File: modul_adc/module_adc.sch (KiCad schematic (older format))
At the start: 26 parts

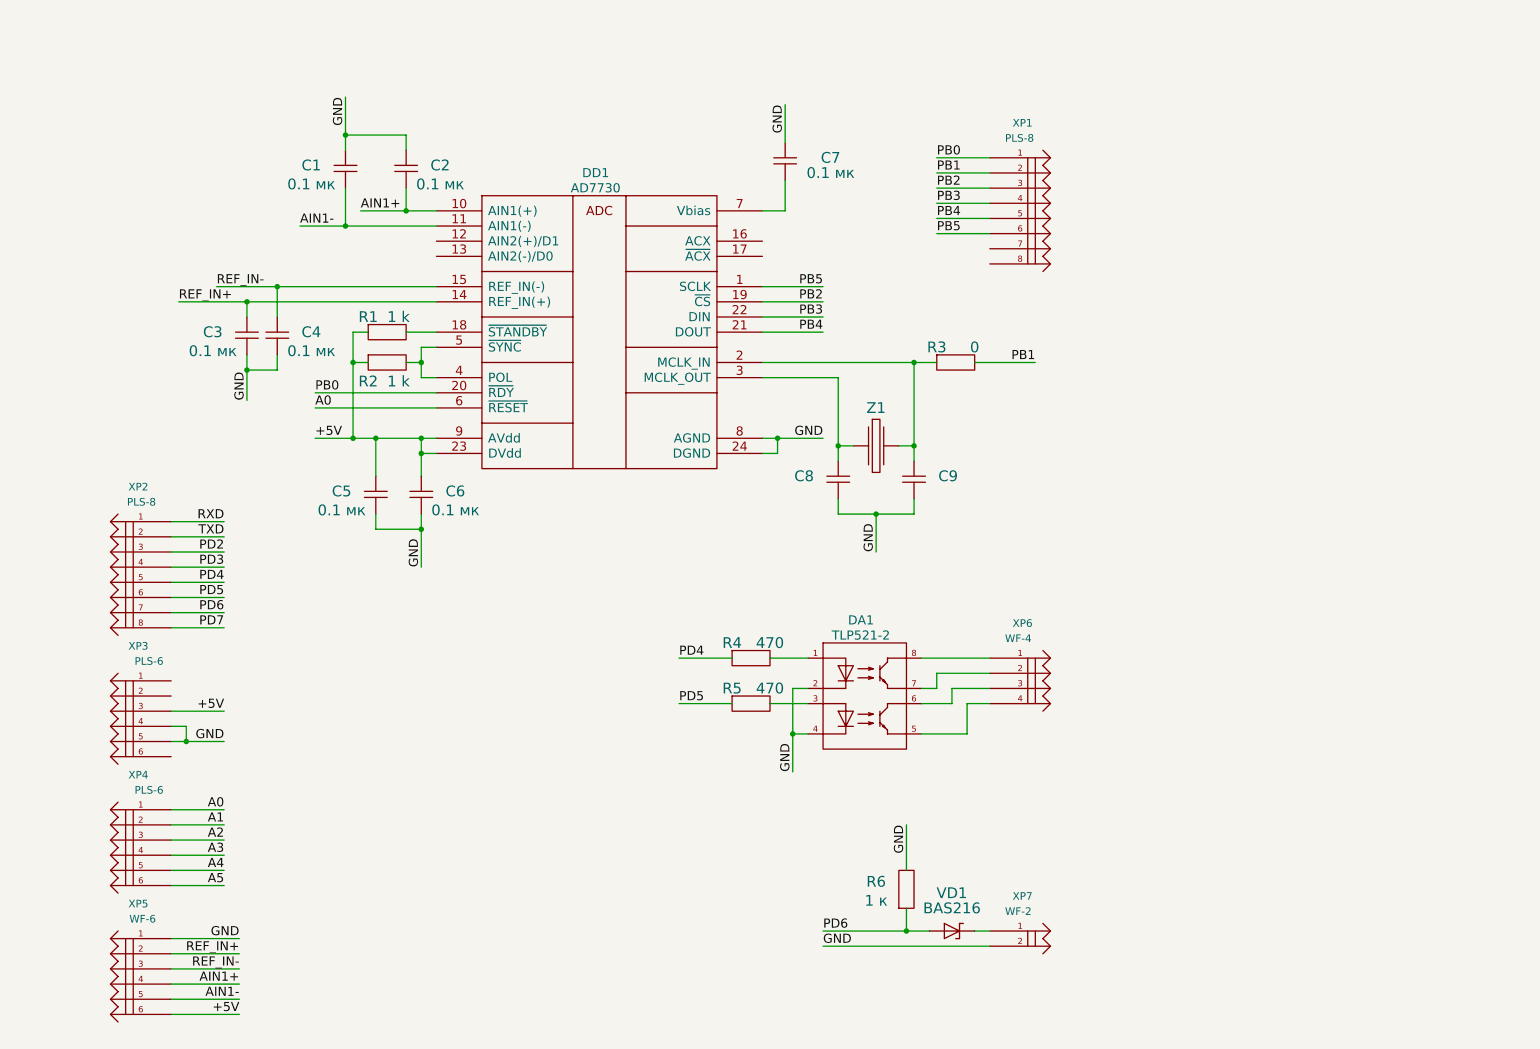
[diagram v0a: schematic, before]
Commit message: Поправил шелкографию и добавил номиналы у элементов для adc_module.
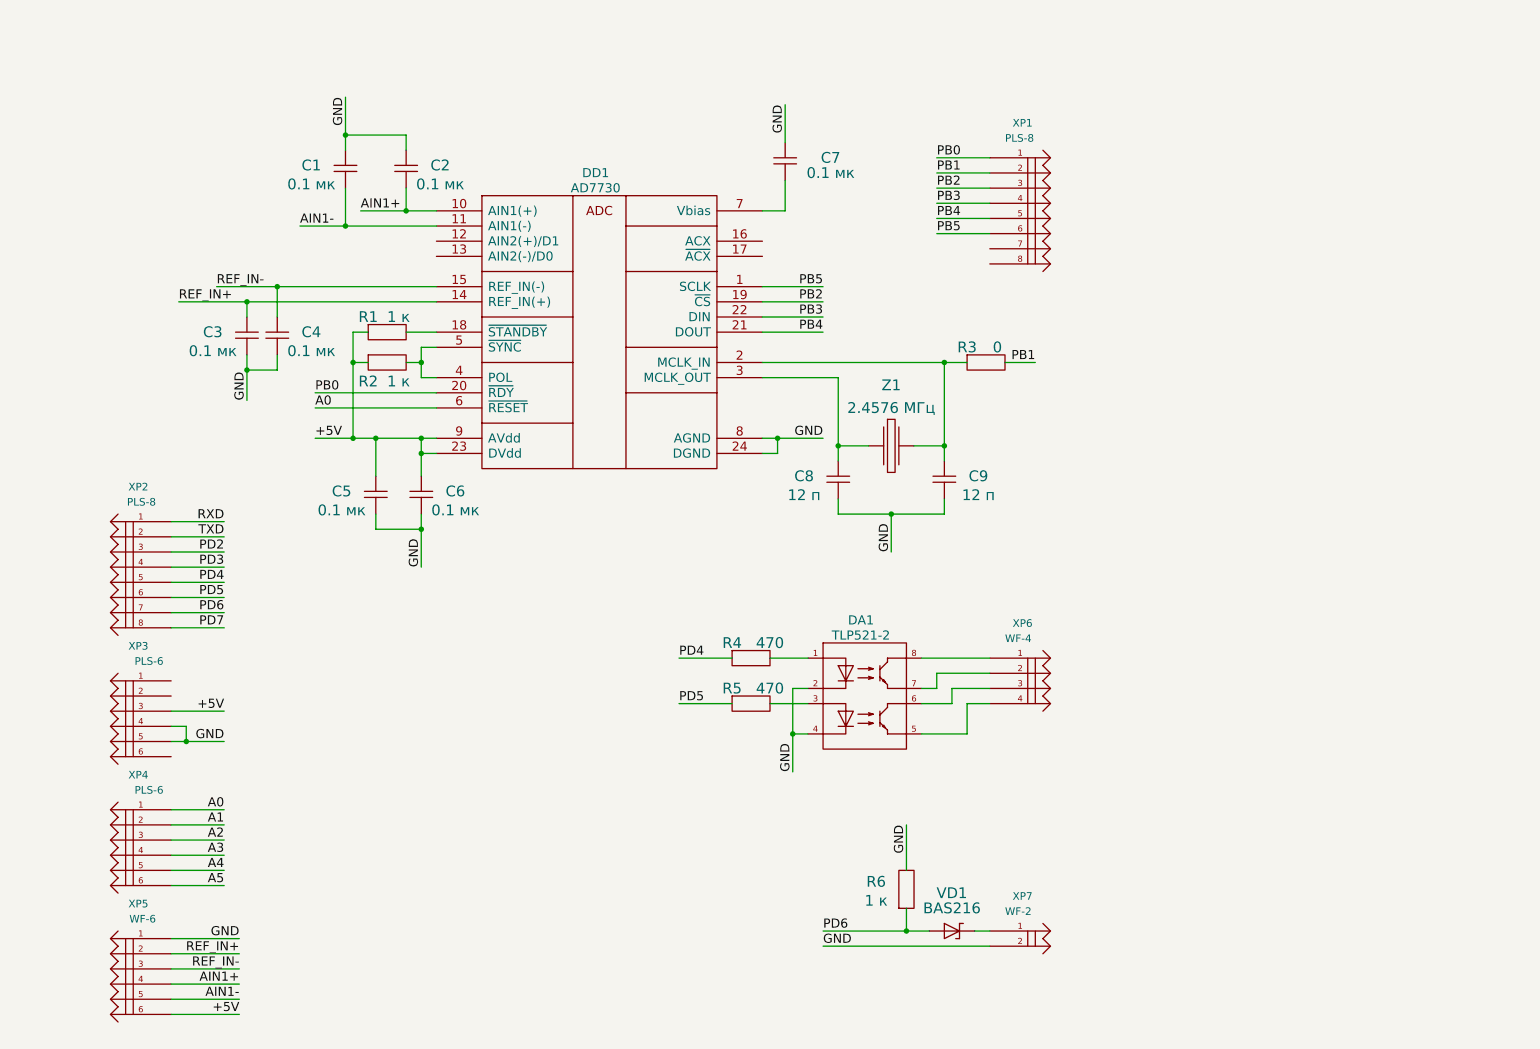
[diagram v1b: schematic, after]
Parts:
- C8, C9: value ~ -> 12 п
- R1, R2: value 1 k -> 1 к
- Z1: value ~ -> 2.4576 МГц
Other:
- moved on the sheet: C9, R3, Z1
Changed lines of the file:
@@
-EESchema Schematic File Version 2  date Thu 03 Apr 2014 16:12:46 MSK
+EESchema Schematic File Version 2
 LIBS:LFcapitors
 LIBS:LFcomponents
@@
 LIBS:LFtransformator
 LIBS:LFbutton
-EELAYER 25  0
+LIBS:module_adc-cache
+EELAYER 27 0
 EELAYER END
-$Descr A4 11700 8267
+$Descr A4 11693 8268
 encoding utf-8
 Sheet 1 1
 Title ""
-Date "3 apr 2014"
+Date "6 nov 2015"
 Rev ""
 Comp ""
@@
 	6100 6900 7200 6900
 Wire Wire Line
-	6800 6800 6100 6800
+	6100 6800 6800 6800
 Wire Wire Line
 	7200 5200 6950 5200
@@
 	6000 5200 5900 5200
 Wire Wire Line
-	6700 3950 6700 4050
-Wire Wire Line
-	6700 4050 6200 4050
+	6900 4050 6900 3950
+Wire Wire Line
+	6200 4050 6900 4050
 Wire Wire Line
 	6200 4050 6200 3950
 Connection ~ 6200 3600
 Wire Wire Line
-	6300 3600 6200 3600
+	6400 3600 6200 3600
 Wire Wire Line
 	5700 3150 6200 3150
@@
 Connection ~ 2950 2150
 Wire Wire Line
-	3550 2150 2650 2150
+	2650 2150 3550 2150
 Wire Wire Line
 	2950 1900 2950 2150
@@
 	2750 3550 3550 3550
 Wire Wire Line
-	6100 3550 5700 3550
+	5700 3550 6100 3550
 Wire Wire Line
 	5850 1350 5850 1600
@@
 	5850 2050 5700 2050
 Wire Wire Line
-	3550 3150 3450 3150
+	3450 3150 3550 3150
 Wire Wire Line
 	6850 2100 7200 2100
@@
 	5700 2550 6100 2550
 Wire Wire Line
-	7100 3050 7500 3050
-Wire Wire Line
-	3450 3150 3450 2950
+	7300 3050 7500 3050
+Wire Wire Line
+	3450 2950 3450 3150
 Wire Wire Line
 	3150 3550 3150 3800
@@
 	3350 1900 3350 2050
 Wire Wire Line
-	3550 2050 3050 2050
+	3050 2050 3550 2050
 Connection ~ 3350 2050
 Wire Wire Line
@@
 Connection ~ 2500 2550
 Wire Wire Line
-	2300 3300 2300 3000
+	2300 3000 2300 3300
 Wire Wire Line
 	2950 1550 3350 1550
@@
 	1800 6400 2150 6400
 Wire Wire Line
-	5700 3050 6850 3050
-Wire Wire Line
-	6700 3700 6700 3050
-Connection ~ 6700 3050
-Wire Wire Line
-	6600 3600 6700 3600
-Connection ~ 6700 3600
-Wire Wire Line
-	6450 4300 6450 4050
-Connection ~ 6450 4050
+	5700 3050 7050 3050
+Wire Wire Line
+	6900 3050 6900 3700
+Connection ~ 6900 3050
+Wire Wire Line
+	6700 3600 6900 3600
+Connection ~ 6900 3600
+Wire Wire Line
+	6550 4300 6550 4050
+Connection ~ 6550 4050
 Wire Wire Line
 	5900 5200 5900 5750
@@
 F 0 "R6" V 6825 6850 71  0000 C CNN
 F 1 "1 к" V 6700 6850 71  0000 C CNN
+F 2 "" H 6650 6650 60  0001 C CNN
+F 3 "" H 6650 6650 60  0001 C CNN
 	1    6650 6650
 	0    -1   -1   0
@@
 F 0 "VD1" H 6950 7050 71  0000 C CNN
 F 1 "BAS216" H 6950 6950 71  0000 C CNN
+F 2 "" H 6800 6800 60  0001 C CNN
+F 3 "" H 6800 6800 60  0001 C CNN
 	1    6800 6800
 	1    0    0    -1
@@
 F 1 "WF-2" H 7300 6900 50  0000 L BNN
 F 2 "~" H 7650 6950 50  0001 C CNN
+F 3 "" H 7200 6800 60  0001 C CNN
 	1    7200 6800
 	1    0    0    -1
@@
 F 1 "WF-4" H 7300 5100 50  0000 L BNN
 F 2 "~" H 7650 5150 50  0001 C CNN
+F 3 "" H 7200 5000 60  0001 C CNN
 	1    7200 5000
 	1    0    0    -1
@@
 F 0 "R5" H 5500 5400 71  0000 C CNN
 F 1 "470" H 5750 5400 71  0000 C CNN
+F 2 "" H 5500 5300 60  0001 C CNN
+F 3 "" H 5500 5300 60  0001 C CNN
 	1    5500 5300
 	1    0    0    -1
@@
 F 0 "R4" H 5500 5100 71  0000 C CNN
 F 1 "470" H 5750 5100 71  0000 C CNN
+F 2 "" H 5500 5000 60  0001 C CNN
+F 3 "" H 5500 5000 60  0001 C CNN
 	1    5500 5000
 	1    0    0    -1
@@
 F 0 "DA1" H 6350 5250 60  0000 C CNN
 F 1 "TLP521-2" H 6350 5150 60  0000 C CNN
+F 2 "" H 6000 5000 60  0001 C CNN
+F 3 "" H 6000 5000 60  0001 C CNN
 	1    6000 5000
 	1    0    0    -1
 $EndComp
-Text Label 6450 4300 1    60   ~ 0
+Text Label 6550 4300 1    60   ~ 0
 GND
 $Comp
@@
 P 6200 3700
 F 0 "C8" V 6300 3925 71  0000 C CNN
-F 1 "~" V 6425 3925 71  0000 C CNN
+F 1 "12 п" V 6425 3925 71  0000 C CNN
+F 2 "" H 6200 3700 60  0001 C CNN
+F 3 "" H 6200 3700 60  0001 C CNN
 	1    6200 3700
 	0    -1   1    0
@@
 L CAPITORS C9
 U 1 1 4ED79054
-P 6700 3700
-F 0 "C9" V 6800 3925 71  0000 C CNN
-F 1 "~" V 6925 3925 71  0000 C CNN
-	1    6700 3700
+P 6900 3700
+F 0 "C9" V 7000 3925 71  0000 C CNN
+F 1 "12 п" V 7125 3925 71  0000 C CNN
+F 2 "" H 6900 3700 60  0001 C CNN
+F 3 "" H 6900 3700 60  0001 C CNN
+	1    6900 3700
 	0    1    1    0
 $EndComp
@@
 L QUARTZ_RESONATOR Z1
 U 1 1 4ED78F56
-P 6300 3600
-F 0 "Z1" H 6450 3850 71  0000 C CNN
-F 1 "~" H 6450 3850 71  0000 C CNN
-	1    6300 3600
+P 6400 3600
+F 0 "Z1" H 6550 4000 71  0000 C CNN
+F 1 "2.4576 МГц" H 6550 3850 71  0000 C CNN
+F 2 "" H 6400 3600 60  0001 C CNN
+F 3 "" H 6400 3600 60  0001 C CNN
+	1    6400 3600
 	1    0    0    -1
 $EndComp
@@
 L RESISTOR R3
 U 1 1 4ED78EB4
-P 6850 3050
-F 0 "R3" H 6850 3150 71  0000 C CNN
-F 1 "0" H 7100 3150 71  0000 C CNN
-	1    6850 3050
+P 7050 3050
+F 0 "R3" H 7050 3150 71  0000 C CNN
+F 1 "0" H 7250 3150 71  0000 C CNN
+F 2 "" H 7050 3050 60  0001 C CNN
+F 3 "" H 7050 3050 60  0001 C CNN
+	1    7050 3050
 	1    0    0    -1
 $EndComp
@@
 F 1 "PLS-6" H 1850 6100 50  0000 L BNN
 F 2 "~" H 2250 6150 50  0001 C CNN
+F 3 "" H 1800 6000 60  0001 C CNN
 	1    1800 6000
 	-1   0    0    -1
@@
 F 1 "PLS-8" H 1900 4200 50  0000 L BNN
 F 2 "~" H 2250 4250 50  0001 C CNN
+F 3 "" H 1800 4100 60  0001 C CNN
 	1    1800 4100
 	-1   0    0    -1
@@
 F 0 "C6" V 3550 4025 71  0000 C CNN
 F 1 "0.1 мк" V 3675 4025 71  0000 C CNN
+F 2 "" H 3450 3800 60  0001 C CNN
+F 3 "" H 3450 3800 60  0001 C CNN
 	1    3450 3800
 	0    1    1    0
@@
 P 3100 2850
 F 0 "R1" H 3100 2950 71  0000 C CNN
-F 1 "1 k" H 3300 2950 71  0000 C CNN
+F 1 "1 к" H 3300 2950 71  0000 C CNN
+F 2 "" H 3100 2850 60  0001 C CNN
+F 3 "" H 3100 2850 60  0001 C CNN
 	1    3100 2850
 	1    0    0    -1
@@
 F 0 "C3" V 2400 2975 71  0000 C CNN
 F 1 "0.1 мк" V 2525 2975 71  0000 C CNN
+F 2 "" H 2300 2750 60  0001 C CNN
+F 3 "" H 2300 2750 60  0001 C CNN
 	1    2300 2750
 	0    -1   1    0
@@
 F 0 "C4" V 2600 2975 71  0000 C CNN
 F 1 "0.1 мк" V 2725 2975 71  0000 C CNN
+F 2 "" H 2500 2750 60  0001 C CNN
+F 3 "" H 2500 2750 60  0001 C CNN
 	1    2500 2750
 	0    1    1    0
@@
 F 1 "WF-6" H 1900 6950 50  0000 L BNN
 F 2 "~" H 2250 7000 50  0001 C CNN
+F 3 "" H 1800 6850 60  0001 C CNN
 	1    1800 6850
 	-1   0    0    -1
@@
 F 0 "C1" V 3050 1875 71  0000 C CNN
 F 1 "0.1 мк" V 3175 1875 71  0000 C CNN
+F 2 "" H 2950 1650 60  0001 C CNN
+F 3 "" H 2950 1650 60  0001 C CNN
 	1    2950 1650
 	0    -1   1    0
@@
 F 0 "C2" V 3450 1875 71  0000 C CNN
 F 1 "0.1 мк" V 3575 1875 71  0000 C CNN
+F 2 "" H 3350 1650 60  0001 C CNN
+F 3 "" H 3350 1650 60  0001 C CNN
 	1    3350 1650
 	0    1    1    0
@@
 F 0 "C5" V 3250 4025 71  0000 C CNN
 F 1 "0.1 мк" V 3375 4025 71  0000 C CNN
+F 2 "" H 3150 3800 60  0001 C CNN
+F 3 "" H 3150 3800 60  0001 C CNN
 	1    3150 3800
 	0    -1   1    0
@@
 F 0 "C7" V 5950 1900 71  0000 C CNN
 F 1 "0.1 мк" V 6050 1900 71  0000 C CNN
+F 2 "" H 5850 1600 60  0001 C CNN
+F 3 "" H 5850 1600 60  0001 C CNN
 	1    5850 1600
 	0    1    1    0
@@
 P 3100 3050
 F 0 "R2" H 3100 2925 71  0000 C CNN
-F 1 "1 k" H 3300 2925 71  0000 C CNN
+F 1 "1 к" H 3300 2925 71  0000 C CNN
+F 2 "" H 3100 3050 60  0001 C CNN
+F 3 "" H 3100 3050 60  0001 C CNN
 	1    3100 3050
 	1    0    0    -1
@@
 F 0 "DD1" H 4600 2100 60  0000 C CNN
 F 1 "AD7730" H 4600 2000 60  0000 C CNN
+F 2 "" H 4100 1950 60  0001 C CNN
+F 3 "" H 4100 1950 60  0001 C CNN
 	1    4100 1950
 	1    0    0    -1
@@
 F 1 "PLS-8" H 7300 1800 50  0000 L BNN
 F 2 "~" H 7650 1850 50  0001 C CNN
+F 3 "" H 7200 1700 60  0001 C CNN
 	1    7200 1700
 	1    0    0    -1
@@
 F 1 "PLS-6" H 1850 5250 50  0000 L BNN
 F 2 "~" H 2250 5300 50  0001 C CNN
+F 3 "" H 1800 5150 60  0001 C CNN
 	1    1800 5150
 	-1   0    0    -1

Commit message: Поправил название микросхемы 74HC595B на 74HC595D.
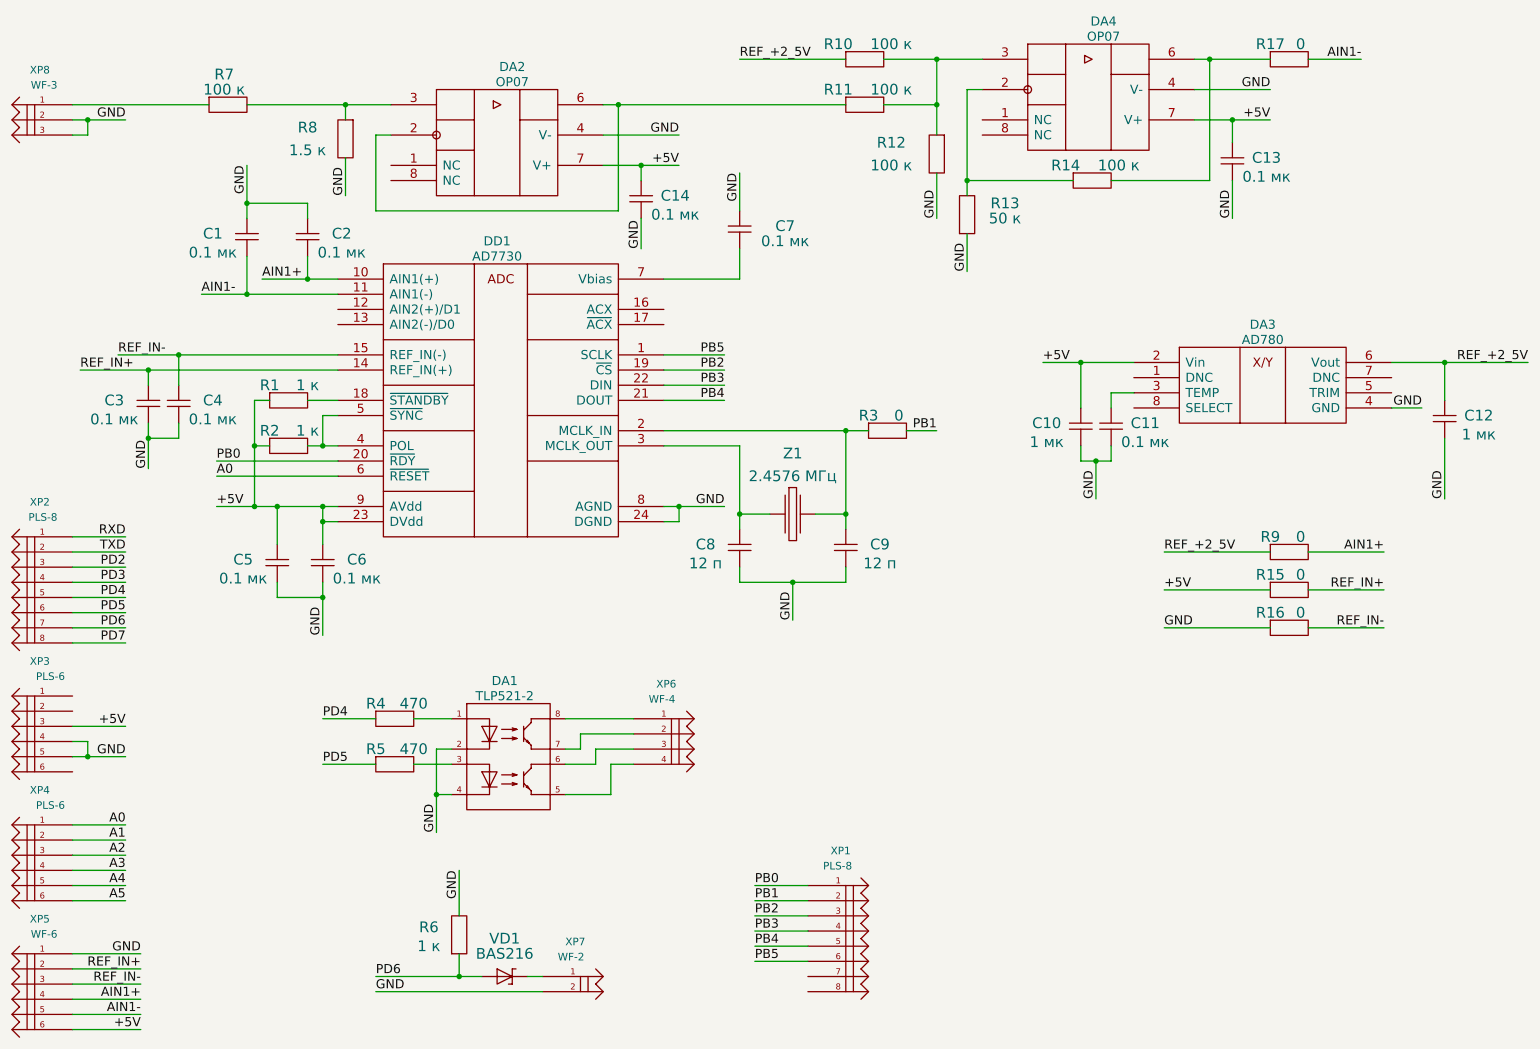
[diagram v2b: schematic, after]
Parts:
- added C10, C12: 1 мк, symbol CAPITORS
- added C11, C13, C14: 0.1 мк, symbol CAPITORS
- added DA2, DA4: OP07, symbol OP07
- added DA3: AD780, symbol AD780
- added R10, R11, R12, R14, R7: 100 к, symbol RESISTOR
- added R13: 50 к, symbol RESISTOR
- added R15, R16, R17, R9: 0, symbol RESISTOR
- added R8: 1.5 к, symbol RESISTOR
- added XP8: WF-3, ~, symbol PIN_M_3
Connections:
- net +5V: now also C10.1, C13.1, C14.1, DA2.7 (V+), DA3.2 (Vin), DA4.7 (V+), R15.1
- net AIN1+: now also R9.2
- net AIN1-: now also R17.2
- net GND: now also C10.2, C11.2, C12.2, C13.2, C14.2, DA2.4 (V-), DA3.4 (GND), DA4.4 (V-), R12.2, R13.1, R16.1, R8.2, XP8.2, XP8.3
- net REF_IN+: now also R15.2
- net REF_IN-: now also R16.2
- new net: C11.1, DA3.3 (TEMP)
- new net: DA4.3, R10.2, R11.2, R12.1
- new net: DA2.2, DA2.6, R11.1
- new net: DA4.2, R13.2, R14.1
- new net: DA4.6, R14.2, R17.1
- new net: R7.1, XP8.1
- new net: DA2.3, R7.2, R8.1
- new net REF_+2_5V: C12.1, DA3.6 (Vout), R10.1, R9.1
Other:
- moved on the sheet: C1, C2, C3, C4, C5, C6, C7, C8, C9, DA1, DD1, R1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
